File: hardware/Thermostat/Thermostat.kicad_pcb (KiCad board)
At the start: 2 copper layers, 106 x 75 mm, 45 parts, among them J1 MainConnectorr, J2 Screw_Terminal_01x02, J3 AVR-ISP-6, K1 G6E, K2 G6E, K3 G6E, K4 G6E, SW1_COOL1 Conn_02x03_Top_Bottom, SW1_FAN1 Conn_02x03_Top_Bottom, SW1_UP1 SW_Push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

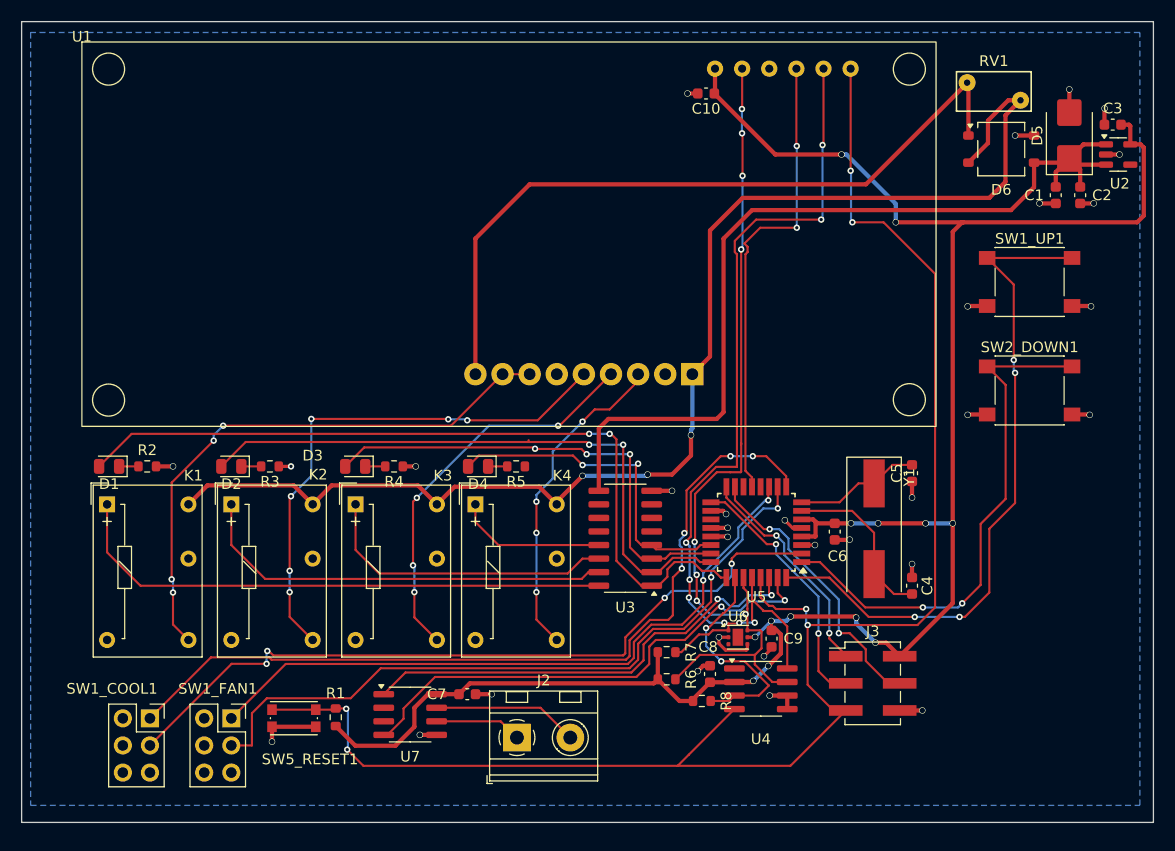
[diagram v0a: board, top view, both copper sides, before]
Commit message: Fix routes and and ERC
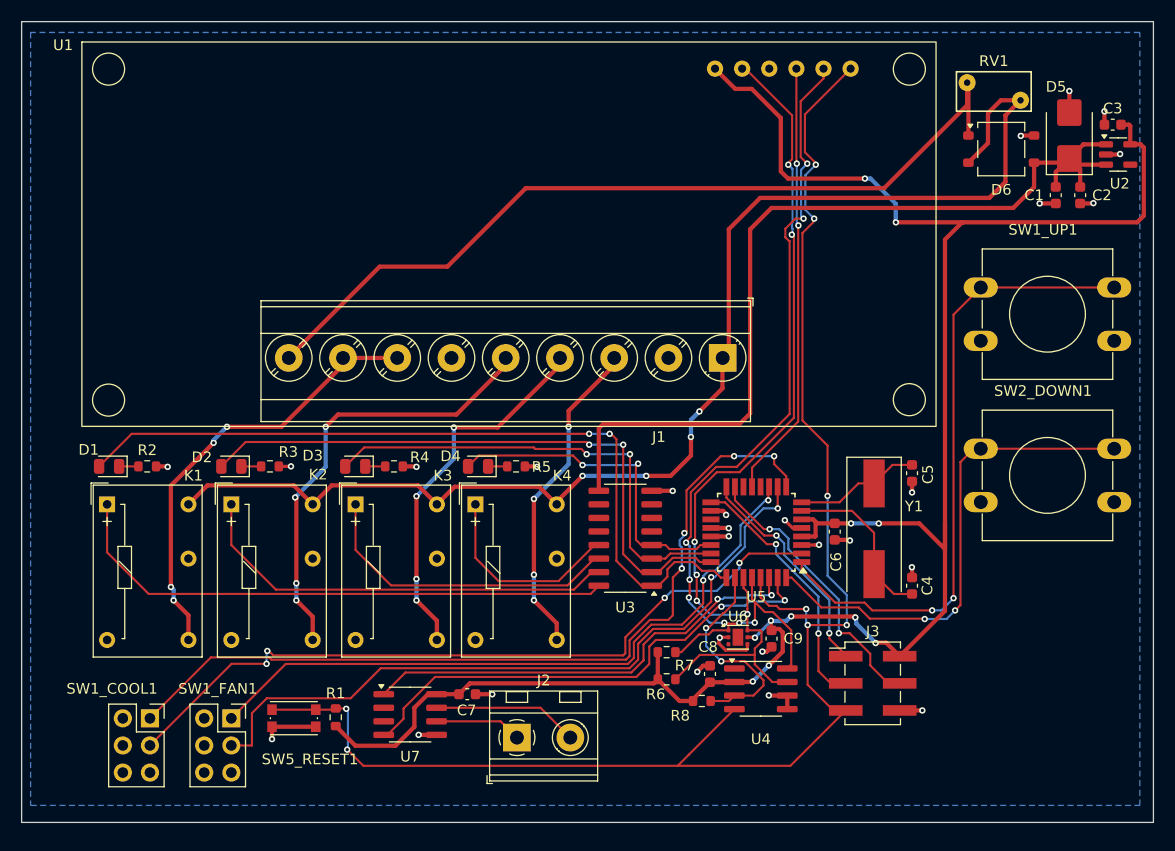
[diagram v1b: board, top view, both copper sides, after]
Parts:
- removed C10: 0.1uF, Capacitor_SMD:C_0603_1608Metric
- J1: footprint TerminalBlock_TE-Connectivity:TerminalBlock_TE_282834-9_1x09_P2.54mm_Horizontal -> TerminalBlock_Phoenix:TerminalBlock_Phoenix_MKDS-3-9-5.08_1x09_P5.08mm_Horizontal; moved to F.Cu
- SW1_UP1, SW2_DOWN1: footprint Button_Switch_SMD:SW_Push_1P1T_NO_6x6mm_H9.5mm -> Button_Switch_THT:SW_PUSH-12mm
- moved SW2_DOWN1 7.12 mm to (207.3, 90.8)
- moved SW1_UP1 4.60 mm to (207.3, 75.7)
- moved J1 3.22 mm to (183.2, 82.3)
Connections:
- SW1_UP1 pad 1: Net-(U5-PD2) -> Net-(U5-PD3)
- SW2_DOWN1 pad 1: Net-(U5-PD3) -> Net-(U5-PD2)
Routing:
- net Net-(U5-PD2): track 62.9 -> 48.1 mm, vias 4 -> 2
- net Net-(J1-Pin_7): track 53.4 -> 41.5 mm
- net 24VAC_N: track 70.0 -> 81.3 mm
- net Net-(U5-PD3): track 49.5 -> 59.6 mm
- net Net-(J1-Pin_5): track 49.8 -> 41.0 mm, vias 6 -> 4
- net GND: track 56.5 -> 47.8 mm, vias 31 -> 27
- net ^RESET: track 154.2 -> 147.1 mm, vias 6 -> 8
- net Net-(U3-OUT4): track 14.1 -> 18.9 mm
- net +5V: track 191.9 -> 196.5 mm, vias 13 -> 11
- net I2C_SDA: track 80.7 -> 84.8 mm, vias 8 -> 6
- net Net-(J1-Pin_4): track 37.6 -> 34.5 mm
- net SCREEN_BUSY: track 43.7 -> 41.0 mm
- net I2C_SCL: track 86.4 -> 84.5 mm
- net Net-(U3-OUT3): track 28.5 -> 29.5 mm
- net Net-(U3-OUT2): track 39.8 -> 40.6 mm
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
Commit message: Tweaks?
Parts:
- J1: moved to B.Cu
- moved J1 0.22 mm to (183.1, 82.5)

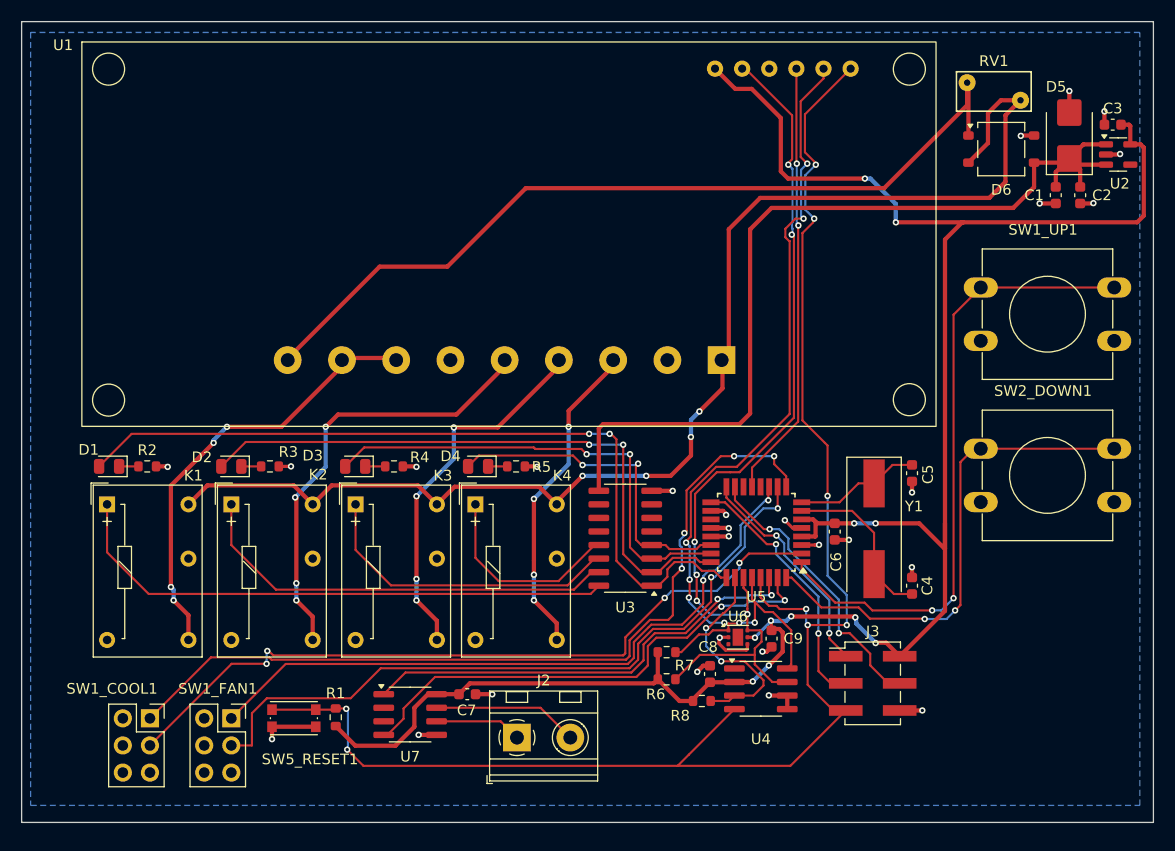
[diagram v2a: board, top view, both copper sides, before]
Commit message: Teardrops, move sensor down, remove lower copper layer
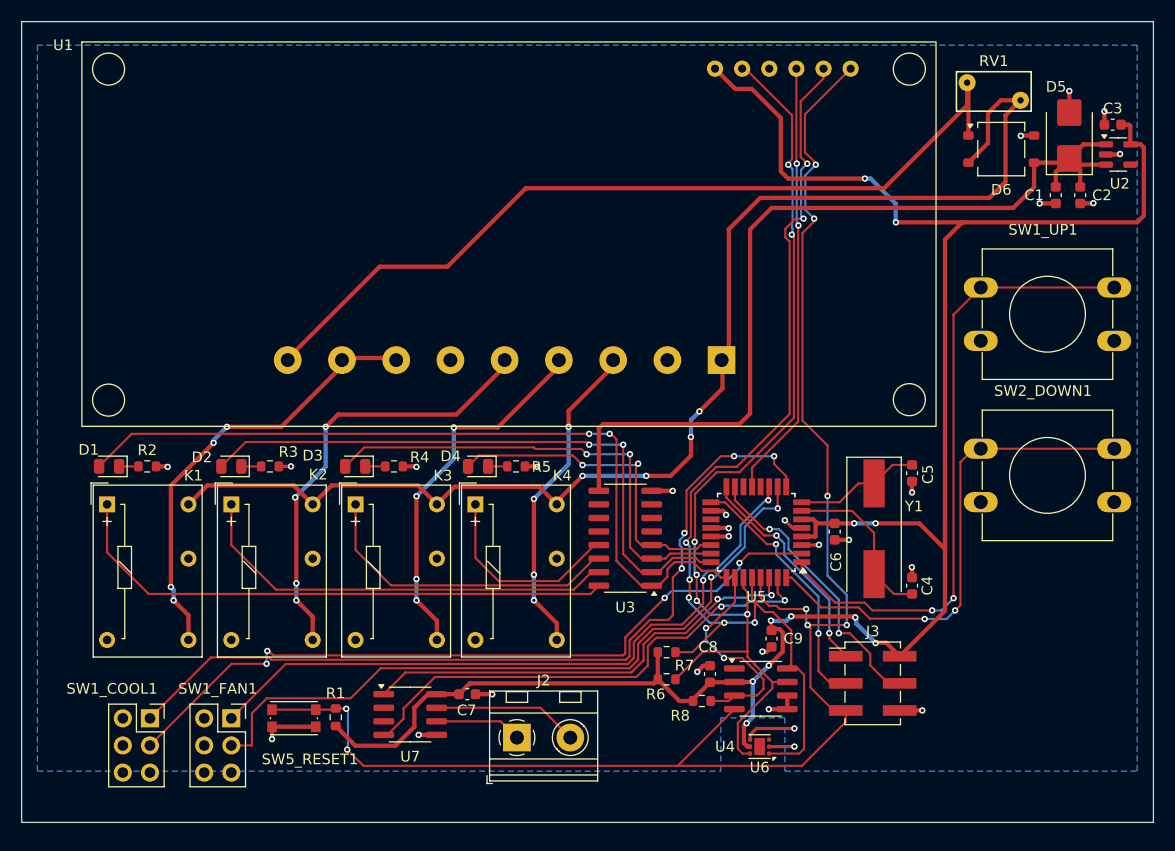
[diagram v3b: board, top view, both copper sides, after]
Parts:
- moved U6 10.4 mm to (186.6, 118.7), turned to 180 degrees
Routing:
- net I2C_SCL: track 84.5 -> 95.9 mm, vias 8 -> 7
- net I2C_SDA: track 84.8 -> 91.9 mm
- net +5V: track 196.5 -> 199.4 mm
- net GND: track 47.8 -> 50.0 mm, vias 27 -> 28
- net Net-(U5-PD2): track 48.1 -> 46.8 mm
- net Net-(SW1_COOL1-Pin_1): track 80.1 -> 79.3 mm
- net 24VAC_N: track 81.3 -> 80.5 mm
- net ^RESET: track 147.1 -> 147.7 mm

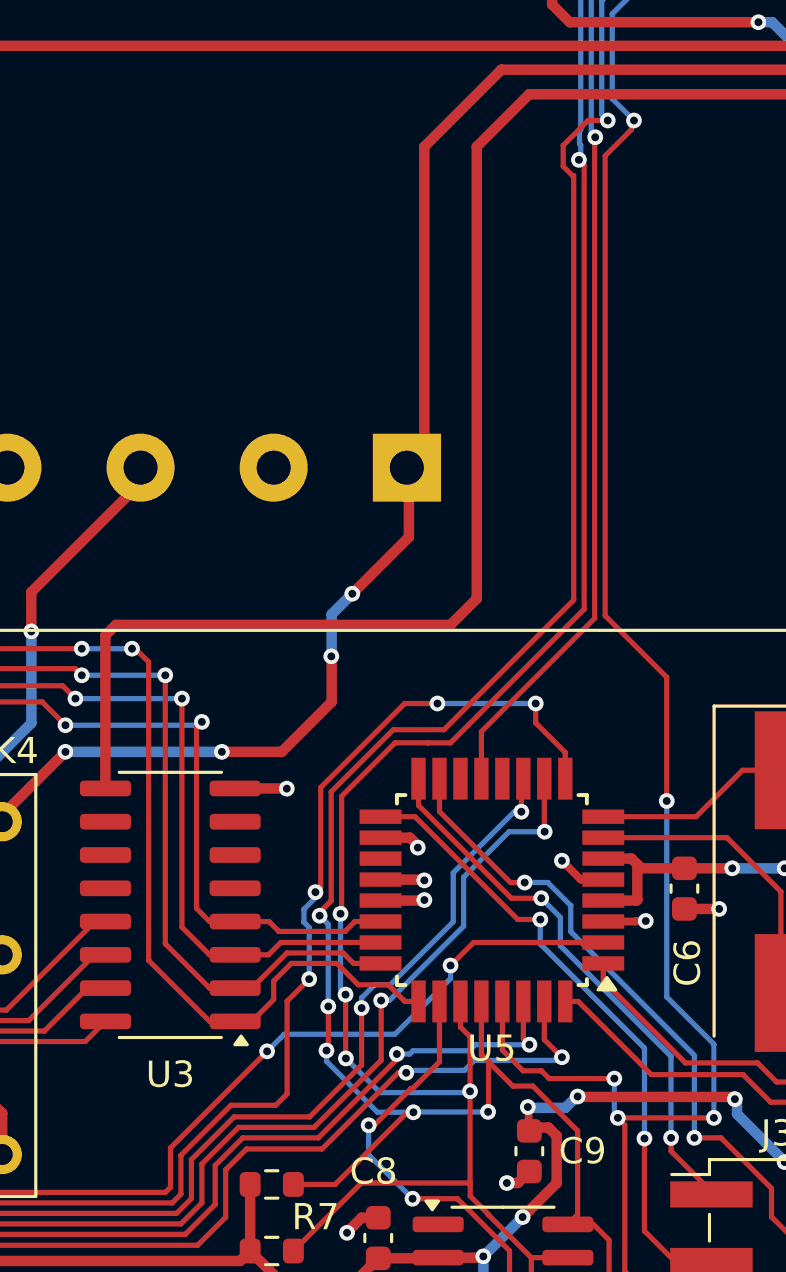
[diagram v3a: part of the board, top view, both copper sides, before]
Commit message: Move Relay thing off of ADC7 and re-route
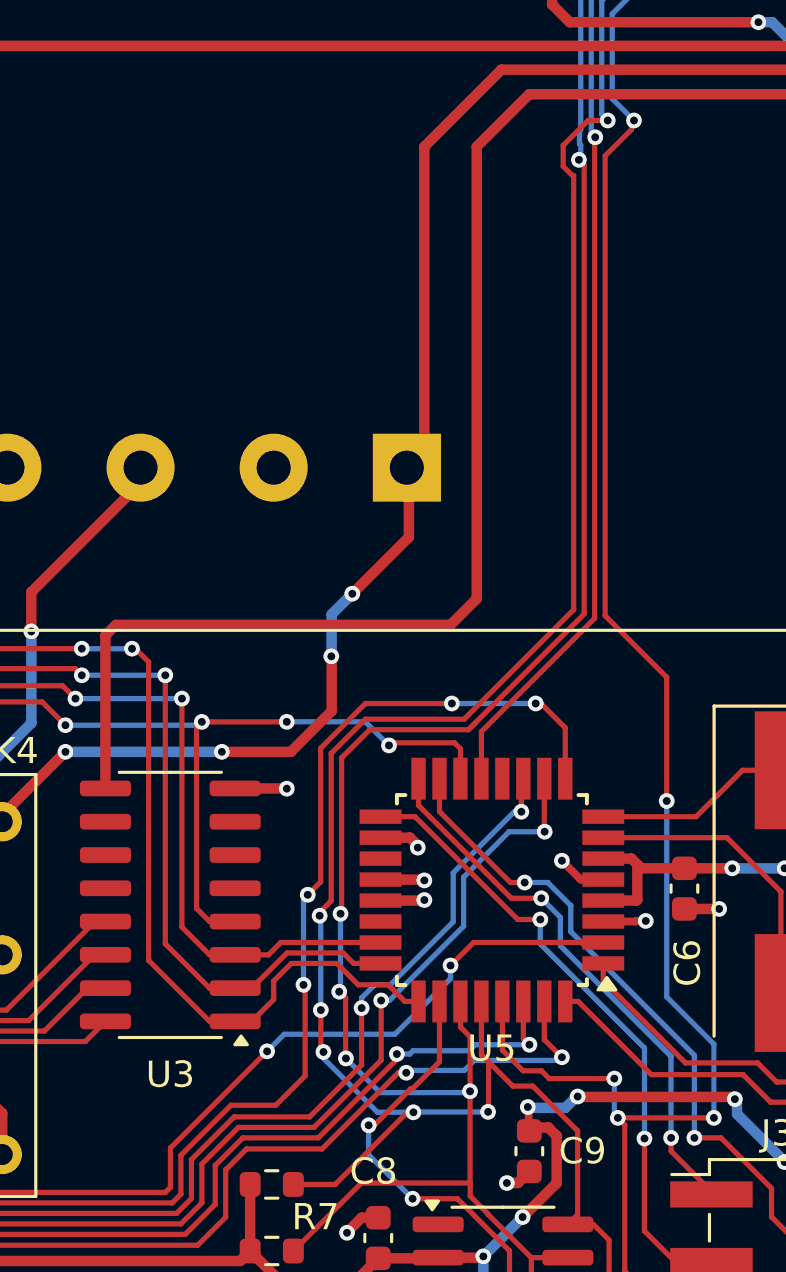
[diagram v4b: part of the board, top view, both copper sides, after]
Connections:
- U5 pad 14: unconnected-(U5-PB2-Pad14) -> Net-(D4-A)
- U5 pad 22: Net-(D4-A) -> unconnected-(U5-ADC7-Pad22)
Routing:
- net Net-(D4-A): track 31.5 -> 37.2 mm, vias 2 -> 4
- net I2C_SDA: track 91.9 -> 93.2 mm
- net I2C_SCL: track 95.9 -> 96.9 mm
- net Net-(SW1_COOL1-Pin_1): track 79.3 -> 80.2 mm

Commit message: Various WIP; Get switches in; Flesh driver; Start simulator
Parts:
- removed SW1_COOL1, SW1_FAN1: Conn_02x03_Top_Bottom, Connector_PinSocket_2.54mm:PinSocket_2x03_P2.54mm_Vertical
- added J4: Conn_01x03_Pin, Connector_PinSocket_2.54mm:PinSocket_1x03_P2.54mm_Vertical, F.Cu at (129.0, 114.5)
- added J5: Conn_01x03_Pin, Connector_PinSocket_2.54mm:PinSocket_1x03_P2.54mm_Vertical, F.Cu at (134.9, 114.5)
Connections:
- U5 pad 11: Net-(SW1_FAN1-Pin_1) -> unconnected-(U5-PD7-Pad11)
- U5 pad 26: RTC_INT -> unconnected-(U5-PC3-Pad26)
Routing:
- net Net-(SW1_FAN1-Pin_1): track 63.5 -> 0.00 mm, vias 2 -> 0
- net Net-(J4-Pin_3): track 70.7 -> 76.5 mm
- net Net-(J5-Pin_3): track 67.5 -> 70.2 mm
- net Net-(J4-Pin_1): track 80.2 -> 81.0 mm

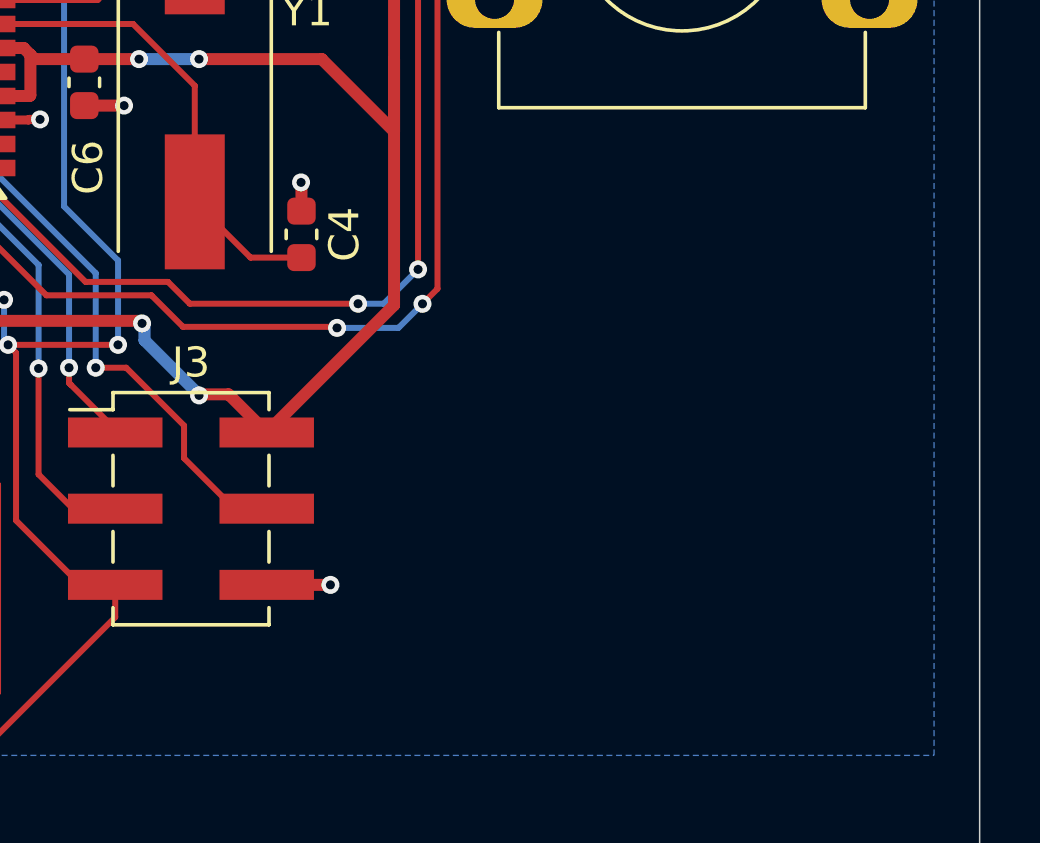
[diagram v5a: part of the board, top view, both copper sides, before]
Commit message: Project upgrade, add program button
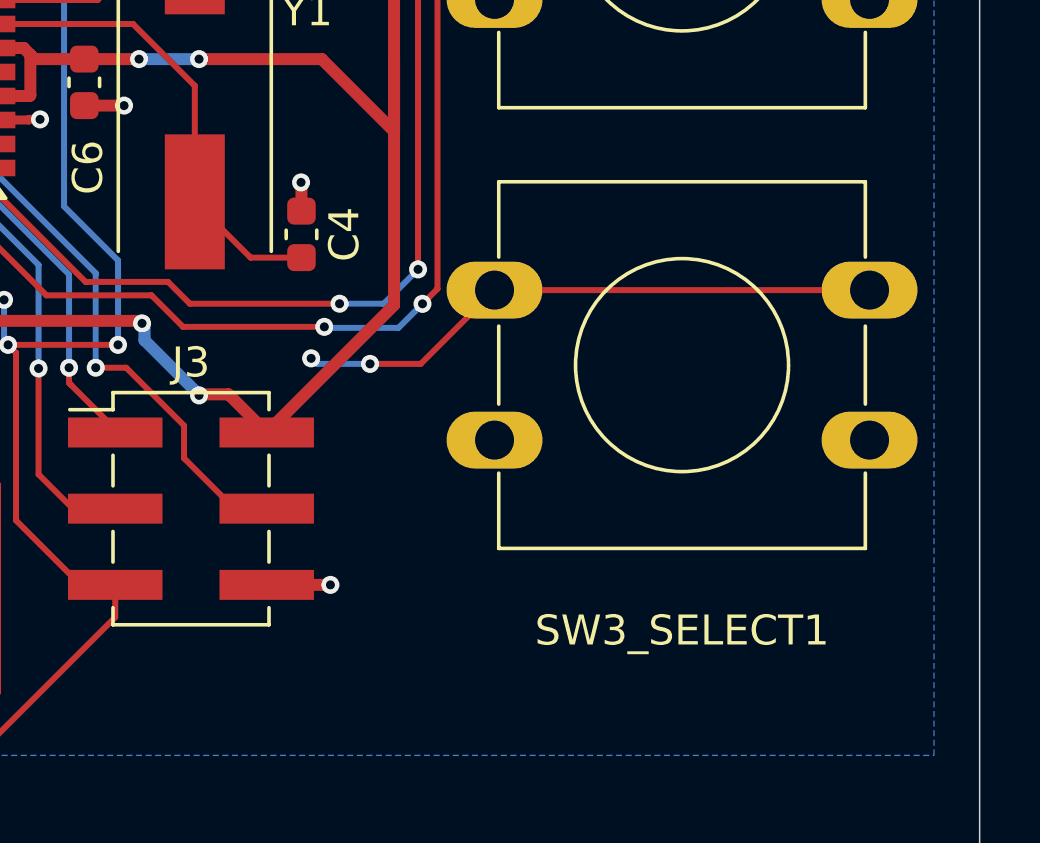
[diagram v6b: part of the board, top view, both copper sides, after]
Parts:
- added SW3_SELECT1: SW_Push, Button_Switch_THT:SW_PUSH-12mm, F.Cu at (207.3, 105.5)
- U4: value DS3231MZ -> DS3232M
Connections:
- U5 pad 11: unconnected-(U5-PD7-Pad11) -> Net-(U5-PD7)
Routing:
- net Net-(U5-PD7): track 0.00 -> 19.8 mm, vias 0 -> 2
